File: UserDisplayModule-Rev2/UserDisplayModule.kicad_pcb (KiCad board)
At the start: 2 copper layers, 162.8 x 84.8 mm, 158 parts, among them J1 RJ45_Shielded, U1 74HC595, U2 LM324, U3 74HC595, U4 74HC595, U5 74HC595, U6 74HC595, U7 74HC595, U8 LM7805_TO220

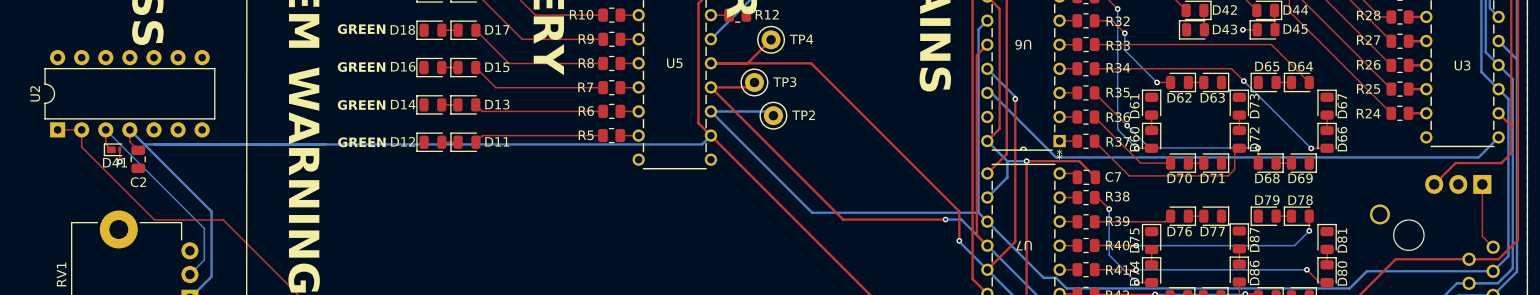
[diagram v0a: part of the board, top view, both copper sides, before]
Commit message: more changes: ldo bypass + grounding op amp
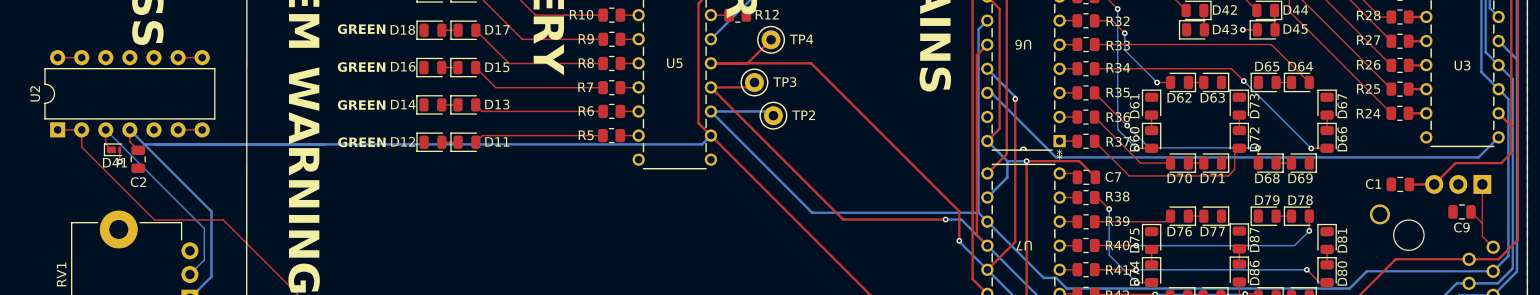
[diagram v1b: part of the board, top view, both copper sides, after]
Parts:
- added C1: 100nF, Capacitor_SMD:C_0805_2012Metric, F.Cu at (214.1, 83.5)
- added C9: 100nF, Capacitor_SMD:C_0805_2012Metric, F.Cu at (220.6, 86.4)
- TP1, TP4: value TestPoint -> TP-RED
- TP2: value TestPoint -> TP-YELLOW
- TP3: value TestPoint -> TP-PURPLE
- TP5: value TestPoint -> TestPoint-YELLOW
- TP6: value TestPoint -> TestPoint-PURPLE
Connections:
- U2 pad 10: (no net) -> GND
- U2 pad 12: (no net) -> GND
- U2 pad 13: (no net) -> Net-(U2D--)
- U2 pad 14: (no net) -> Net-(U2D--)
- U2 pad 5: (no net) -> GND
- U2 pad 6: (no net) -> Net-(U2B--)
- U2 pad 7: (no net) -> Net-(U2B--)
- U2 pad 8: (no net) -> Net-(U2C--)
- U2 pad 9: (no net) -> Net-(U2C--)
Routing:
- net 5V: track 370.8 -> 373.4 mm
- net Net-(U2C--): track 0.00 -> 2.54 mm
- net Net-(U2B--): track 0.00 -> 2.54 mm
- net Net-(U2D--): track 0.00 -> 2.54 mm
- net Net-(U8-VI): track 7.09 -> 8.79 mm
